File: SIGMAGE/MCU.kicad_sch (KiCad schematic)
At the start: 28 parts, among them J10 TSW10607GS, J11 HTSW10807GD, J12 HTSW10807GD, J13 HTSW10807GD, J9 TSW10607GS, U8 STM32F407VGTx, X1 STDCSU18M

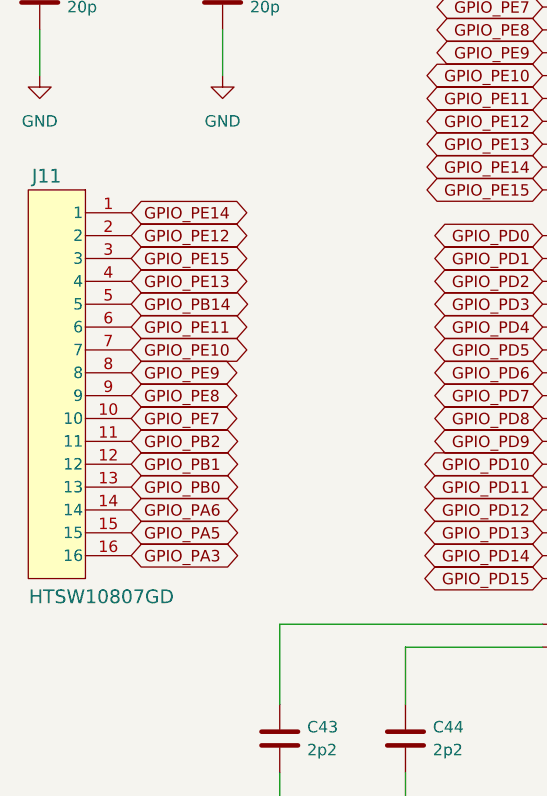
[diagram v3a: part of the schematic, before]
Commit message: Final touches, PCB layout is still horrible, will fix in MK II
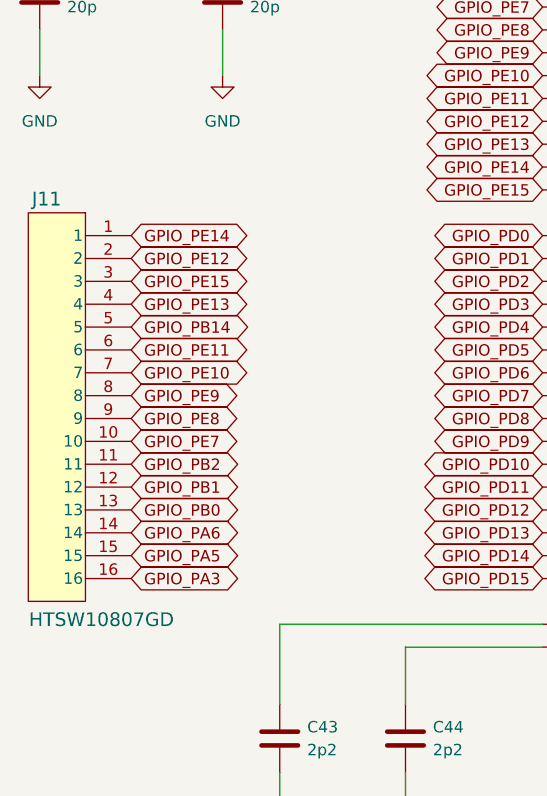
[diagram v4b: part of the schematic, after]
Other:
- moved on the sheet: J11
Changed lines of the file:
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@@
 	(global_label "GPIO_PE9"
 		(shape bidirectional)
-		(at 31.75 124.46 0)
+		(at 31.75 127 0)
 		(fields_autoplaced yes)
 		(effects
@@
 		)
 		(property "Intersheetrefs" "${INTERSHEET_REFS}"
-			(at 44.9179 124.46 0)
+			(at 44.9179 127 0)
 			(effects
 				(font
@@
 	(global_label "GPIO_PB0"
 		(shape bidirectional)
-		(at 31.75 137.16 0)
+		(at 31.75 139.7 0)
 		(fields_autoplaced yes)
 		(effects
@@
 		)
 		(property "Intersheetrefs" "${INTERSHEET_REFS}"
-			(at 45.0389 137.16 0)
+			(at 45.0389 139.7 0)
 			(effects
 				(font
@@
 	(global_label "GPIO_PE12"
 		(shape bidirectional)
-		(at 31.75 109.22 0)
+		(at 31.75 111.76 0)
 		(fields_autoplaced yes)
 		(effects
@@
 		)
 		(property "Intersheetrefs" "${INTERSHEET_REFS}"
-			(at 46.1274 109.22 0)
+			(at 46.1274 111.76 0)
 			(effects
 				(font
@@
 	(global_label "GPIO_PA6"
 		(shape bidirectional)
-		(at 31.75 139.7 0)
+		(at 31.75 142.24 0)
 		(fields_autoplaced yes)
 		(effects
@@
 		)
 		(property "Intersheetrefs" "${INTERSHEET_REFS}"
-			(at 44.8575 139.7 0)
+			(at 44.8575 142.24 0)
 			(effects
 				(font
@@
 	(global_label "GPIO_PA5"
 		(shape bidirectional)
-		(at 31.75 142.24 0)
+		(at 31.75 144.78 0)
 		(fields_autoplaced yes)
 		(effects
@@
 		)
 		(property "Intersheetrefs" "${INTERSHEET_REFS}"
-			(at 44.8575 142.24 0)
+			(at 44.8575 144.78 0)
 			(effects
 				(font
@@
 	(global_label "GPIO_PB14"
 		(shape bidirectional)
-		(at 31.75 116.84 0)
+		(at 31.75 119.38 0)
 		(fields_autoplaced yes)
 		(effects
@@
 		)
 		(property "Intersheetrefs" "${INTERSHEET_REFS}"
-			(at 46.2484 116.84 0)
+			(at 46.2484 119.38 0)
 			(effects
 				(font
@@
 	(global_label "GPIO_PB1"
 		(shape bidirectional)
-		(at 31.75 134.62 0)
+		(at 31.75 137.16 0)
 		(fields_autoplaced yes)
 		(effects
@@
 		)
 		(property "Intersheetrefs" "${INTERSHEET_REFS}"
-			(at 45.0389 134.62 0)
+			(at 45.0389 137.16 0)
 			(effects
 				(font
@@
 	(global_label "GPIO_PB2"
 		(shape bidirectional)
-		(at 31.75 132.08 0)
+		(at 31.75 134.62 0)
 		(fields_autoplaced yes)
 		(effects
@@
 		)
 		(property "Intersheetrefs" "${INTERSHEET_REFS}"
-			(at 45.0389 132.08 0)
+			(at 45.0389 134.62 0)
 			(effects
 				(font
@@
 	(global_label "GPIO_PE14"
 		(shape bidirectional)
-		(at 31.75 106.68 0)
+		(at 31.75 109.22 0)
 		(fields_autoplaced yes)
 		(effects
@@
 		)
 		(property "Intersheetrefs" "${INTERSHEET_REFS}"
-			(at 46.1274 106.68 0)
+			(at 46.1274 109.22 0)
 			(effects
 				(font
@@
 	(global_label "GPIO_PE11"
 		(shape bidirectional)
-		(at 31.75 119.38 0)
+		(at 31.75 121.92 0)
 		(fields_autoplaced yes)
 		(effects
@@
 		)
 		(property "Intersheetrefs" "${INTERSHEET_REFS}"
-			(at 46.1274 119.38 0)
+			(at 46.1274 121.92 0)
 			(effects
 				(font
@@
 	(global_label "GPIO_PE7"
 		(shape bidirectional)
-		(at 31.75 129.54 0)
+		(at 31.75 132.08 0)
 		(fields_autoplaced yes)
 		(effects
@@
 		)
 		(property "Intersheetrefs" "${INTERSHEET_REFS}"
-			(at 44.9179 129.54 0)
+			(at 44.9179 132.08 0)
 			(effects
 				(font
@@
 	(global_label "GPIO_PE13"
 		(shape bidirectional)
-		(at 31.75 114.3 0)
+		(at 31.75 116.84 0)
 		(fields_autoplaced yes)
 		(effects
@@
 		)
 		(property "Intersheetrefs" "${INTERSHEET_REFS}"
-			(at 46.1274 114.3 0)
+			(at 46.1274 116.84 0)
 			(effects
 				(font
@@
 	(global_label "GPIO_PE15"
 		(shape bidirectional)
-		(at 31.75 111.76 0)
+		(at 31.75 114.3 0)
 		(fields_autoplaced yes)
 		(effects
@@
 		)
 		(property "Intersheetrefs" "${INTERSHEET_REFS}"
-			(at 46.1274 111.76 0)
+			(at 46.1274 114.3 0)
 			(effects
 				(font
@@
 	(global_label "GPIO_PE8"
 		(shape bidirectional)
-		(at 31.75 127 0)
+		(at 31.75 129.54 0)
 		(fields_autoplaced yes)
 		(effects
@@
 		)
 		(property "Intersheetrefs" "${INTERSHEET_REFS}"
-			(at 44.9179 127 0)
+			(at 44.9179 129.54 0)
 			(effects
 				(font
@@
 	(global_label "GPIO_PA3"
 		(shape bidirectional)
-		(at 31.75 144.78 0)
+		(at 31.75 147.32 0)
 		(fields_autoplaced yes)
 		(effects
@@
 		)
 		(property "Intersheetrefs" "${INTERSHEET_REFS}"
-			(at 44.8575 144.78 0)
+			(at 44.8575 147.32 0)
 			(effects
 				(font
@@
 	(global_label "GPIO_PE10"
 		(shape bidirectional)
-		(at 31.75 121.92 0)
+		(at 31.75 124.46 0)
 		(fields_autoplaced yes)
 		(effects
@@
 		)
 		(property "Intersheetrefs" "${INTERSHEET_REFS}"
-			(at 46.1274 121.92 0)
+			(at 46.1274 124.46 0)
 			(effects
 				(font
@@
 	(symbol
 		(lib_id "SIGMAGE:HTSW10807GD")
-		(at 26.67 104.14 0)
+		(at 26.67 106.68 0)
 		(mirror y)
 		(unit 1)
@@
 		(dnp no)
 		(property "Reference" "J11"
-			(at 22.352 102.616 0)
+			(at 22.352 105.156 0)
 			(effects
 				(font
@@
 		)
 		(property "Value" "HTSW10807GD"
-			(at 28.448 149.352 0)
+			(at 28.448 151.892 0)
 			(effects
 				(font
@@
 		)
 		(property "Footprint" "SIGMAGE:HTSW10807GD"
-			(at 25.4 99.06 0)
+			(at 25.4 101.6 0)
 			(effects
 				(font
@@
 		)
 		(property "Datasheet" "HTSW-108-07-G-D"
-			(at 25.146 96.774 0)
+			(at 25.146 99.314 0)
 			(effects
 				(font
@@
 		)
 		(property "Description" "HTSW10807GD"
-			(at 25.146 94.488 0)
+			(at 25.146 97.028 0)
 			(effects
 				(font

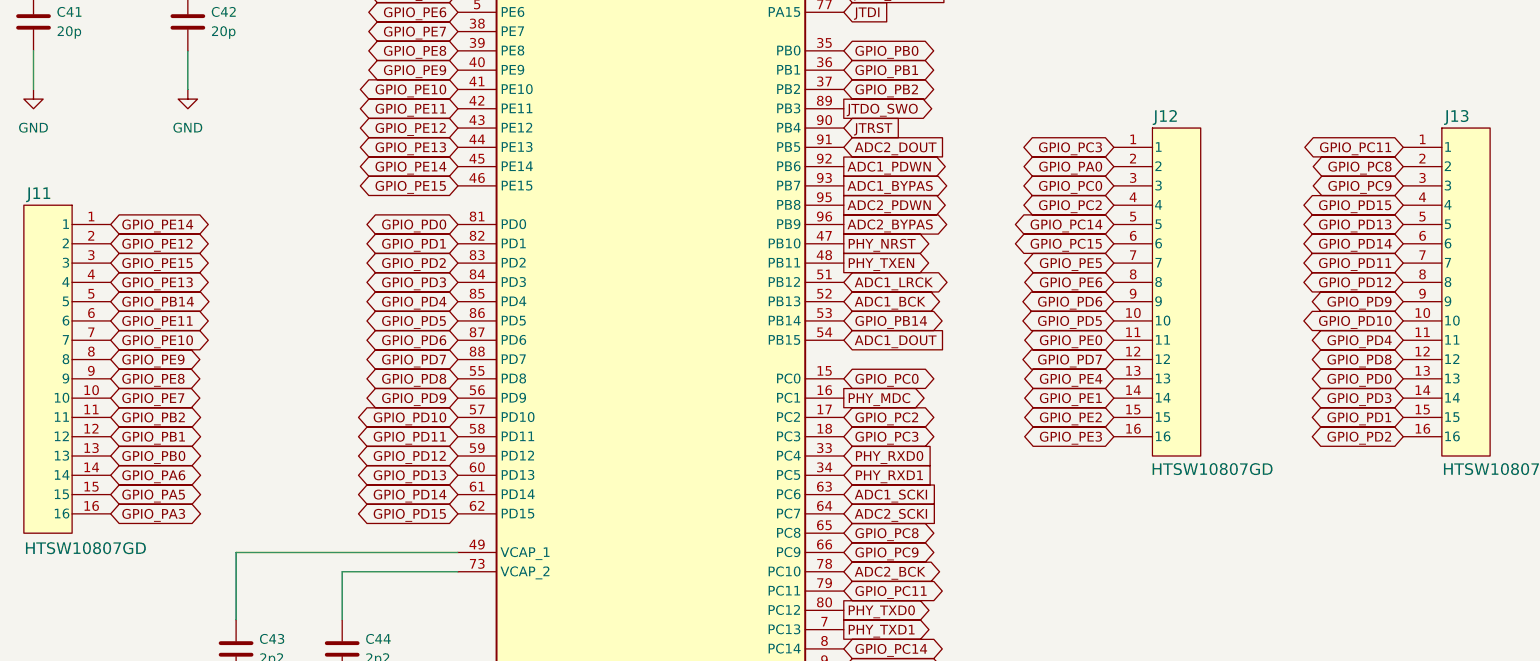
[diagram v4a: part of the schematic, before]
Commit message: Makin it waaay cheaper and JLCPCB conform
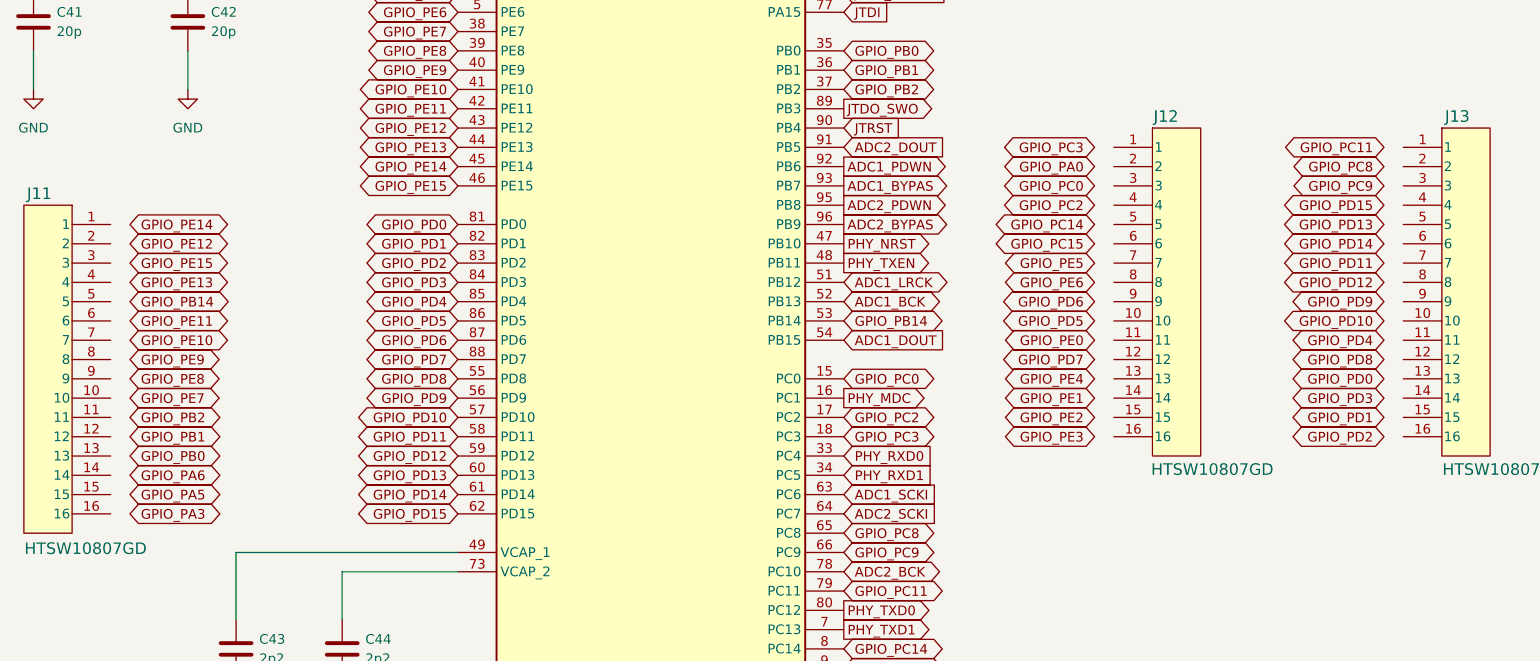
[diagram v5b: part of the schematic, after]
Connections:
- net GPIO_PA0: no longer J12.2
- net GPIO_PA3: no longer J11.16
- net GPIO_PA5: no longer J11.15
- net GPIO_PA6: no longer J11.14
- net GPIO_PB0: no longer J11.13
- net GPIO_PB1: no longer J11.12
- net GPIO_PB14: no longer J11.5
- net GPIO_PB2: no longer J11.11
- net GPIO_PC0: no longer J12.3
- net GPIO_PC11: no longer J13.1
- net GPIO_PC14: no longer J12.5
- net GPIO_PC15: no longer J12.6
- net GPIO_PC2: no longer J12.4
- net GPIO_PC3: no longer J12.1
- net GPIO_PC8: no longer J13.2
- net GPIO_PC9: no longer J13.3
- net GPIO_PD0: no longer J13.13
- net GPIO_PD1: no longer J13.15
- net GPIO_PD10: no longer J13.10
- net GPIO_PD11: no longer J13.7
- net GPIO_PD12: no longer J13.8
- net GPIO_PD13: no longer J13.5
- net GPIO_PD14: no longer J13.6
- net GPIO_PD15: no longer J13.4
- net GPIO_PD2: no longer J13.16
- net GPIO_PD3: no longer J13.14
- net GPIO_PD4: no longer J13.11
- net GPIO_PD5: no longer J12.10
- net GPIO_PD6: no longer J12.9
- net GPIO_PD7: no longer J12.12
- net GPIO_PD8: no longer J13.12
- net GPIO_PD9: no longer J13.9
- net GPIO_PE0: no longer J12.11
- net GPIO_PE1: no longer J12.14
- net GPIO_PE10: no longer J11.7
- net GPIO_PE11: no longer J11.6
- net GPIO_PE12: no longer J11.2
- net GPIO_PE13: no longer J11.4
- net GPIO_PE14: no longer J11.1
- net GPIO_PE15: no longer J11.3
- net GPIO_PE2: no longer J12.15
- net GPIO_PE3: no longer J12.16
- net GPIO_PE4: no longer J12.13
- net GPIO_PE5: no longer J12.7
- net GPIO_PE6: no longer J12.8
- net GPIO_PE7: no longer J11.10
- net GPIO_PE8: no longer J11.9
- net GPIO_PE9: no longer J11.8
